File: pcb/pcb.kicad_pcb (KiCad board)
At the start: 2 copper layers, 48 x 60 mm, 51 parts, among them J1 USB_C_Receptacle_USB2.0_14P, J2 LCD, J4 LCD CTRL, J5 Moisture, J6 HC-05, J7 DEBUG, J9 USART3 TX, SW1 PWR SWITCH, U1 TLV62569DBV, U2 STM32F446RETx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

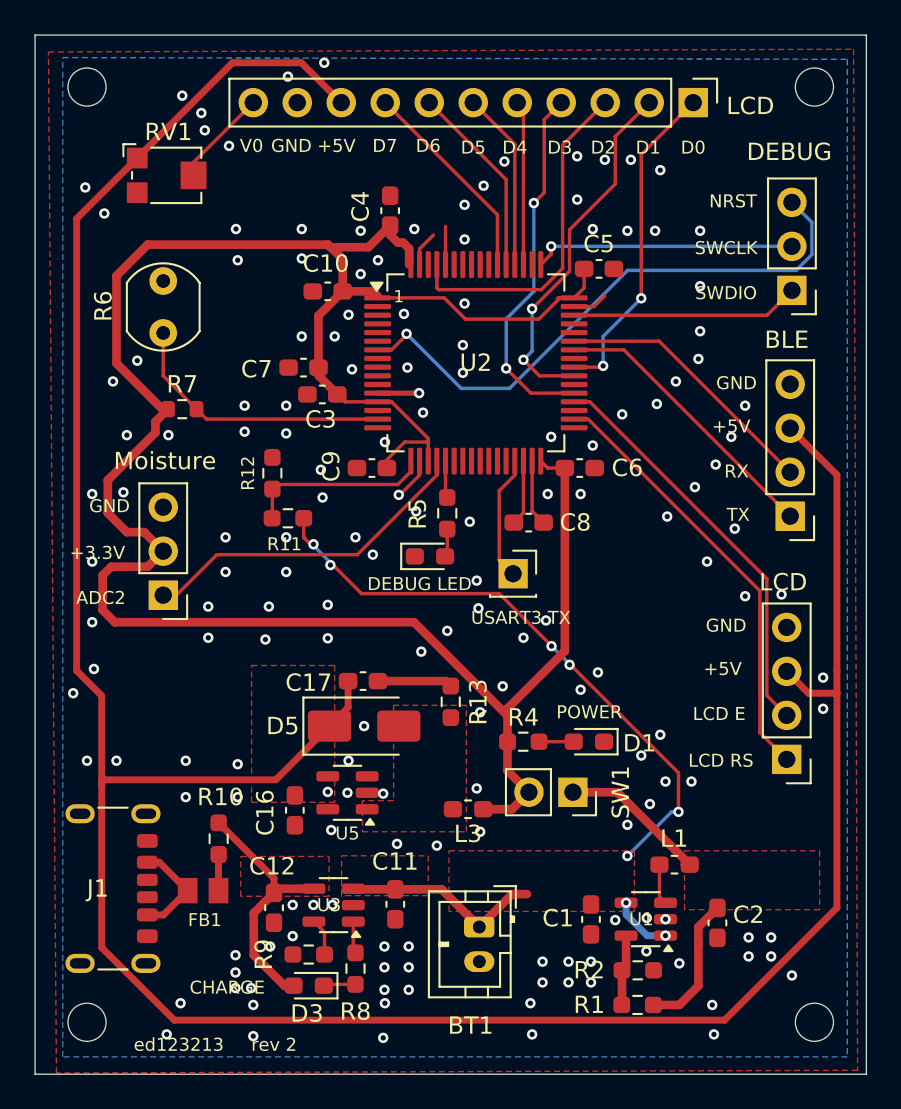
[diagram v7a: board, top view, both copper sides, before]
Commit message: Add more vias
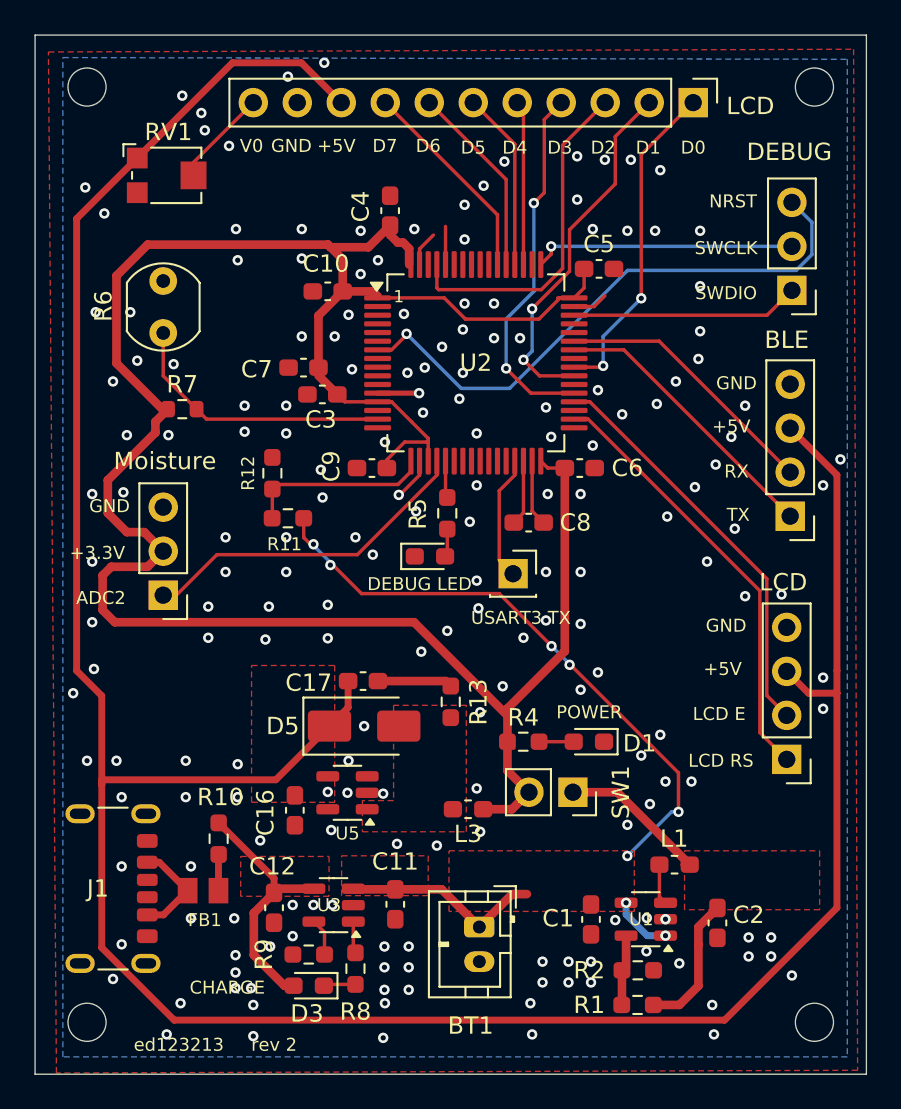
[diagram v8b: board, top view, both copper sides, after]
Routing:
- net GND: vias 166 -> 192
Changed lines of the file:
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@@
+	)
+	(via
+		(at 73 90.5)
+		(size 0.6)
+		(drill 0.3)
+		(layers "F.Cu" "B.Cu")
+		(free yes)
+		(net 1)
+	)
+	(via
+		(at 73 87.5)
+		(size 0.6)
+		(drill 0.3)
+		(layers "F.Cu" "B.Cu")
+		(free yes)
+		(net 1)
 	)
 	(via
@@
 	)
 	(via
+		(at 69 92)
+		(size 0.6)
+		(drill 0.3)
+		(layers "F.Cu" "B.Cu")
+		(free yes)
+		(net 1)
+	)
+	(via
 		(at 78.5 70.5)
 		(size 0.6)
@@
 	)
 	(via
+		(at 69.5 55.5)
+		(size 0.6)
+		(drill 0.3)
+		(layers "F.Cu" "B.Cu")
+		(free yes)
+		(net 1)
+	)
+	(via
 		(at 109.5 76.6)
 		(size 0.6)
@@
 	)
 	(via
+		(at 95.5 70.5)
+		(size 0.6)
+		(drill 0.3)
+		(layers "F.Cu" "B.Cu")
+		(free yes)
+		(net 1)
+	)
+	(via
+		(at 92 57)
+		(size 0.6)
+		(drill 0.3)
+		(layers "F.Cu" "B.Cu")
+		(free yes)
+		(net 1)
+	)
+	(via
 		(at 85.574 93.326)
 		(size 0.6)
@@
 	)
 	(via
+		(at 75.5 90.5)
+		(size 0.6)
+		(drill 0.3)
+		(layers "F.Cu" "B.Cu")
+		(free yes)
+		(net 1)
+	)
+	(via
 		(at 80.9 83.2)
 		(size 0.6)
@@
 	)
 	(via
+		(at 89.5 65.5)
+		(size 0.6)
+		(drill 0.3)
+		(layers "F.Cu" "B.Cu")
+		(free yes)
+		(net 1)
+	)
+	(via
 		(at 89.6 72.6)
 		(size 0.6)
@@
 	)
 	(via
+		(at 67.5 55.5)
+		(size 0.6)
+		(drill 0.3)
+		(layers "F.Cu" "B.Cu")
+		(free yes)
+		(net 1)
+	)
+	(via
 		(at 80.5 64.6)
 		(size 0.6)
@@
 	)
 	(via
+		(at 88.5 60.5)
+		(size 0.6)
+		(drill 0.3)
+		(layers "F.Cu" "B.Cu")
+		(free yes)
+		(net 1)
+	)
+	(via
 		(at 76.1 62.4)
 		(size 0.6)
@@
 	)
 	(via
-		(at 85.5 58.7)
+		(at 86.5 58.7)
 		(size 0.6)
 		(drill 0.3)
@@
 	)
 	(via
+		(at 95.5 73.5)
+		(size 0.6)
+		(drill 0.3)
+		(layers "F.Cu" "B.Cu")
+		(free yes)
+		(net 1)
+	)
+	(via
 		(at 93.5 73.3)
 		(size 0.6)
@@
 	)
 	(via
+		(at 93.5 70.5)
+		(size 0.6)
+		(drill 0.3)
+		(layers "F.Cu" "B.Cu")
+		(free yes)
+		(net 1)
+	)
+	(via
 		(at 75.574 92.626)
 		(size 0.6)
@@
 	)
 	(via
+		(at 77 86)
+		(size 0.6)
+		(drill 0.3)
+		(layers "F.Cu" "B.Cu")
+		(free yes)
+		(net 1)
+	)
+	(via
 		(at 82.0375 83.25)
 		(size 0.6)
@@
 	)
 	(via
+		(at 109.5 65.5)
+		(size 0.6)
+		(drill 0.3)
+		(layers "F.Cu" "B.Cu")
+		(free yes)
+		(net 1)
+	)
+	(via
 		(at 75.7 52.5)
 		(size 0.6)
@@
 	)
 	(via
-		(at 88.7 57.4)
+		(at 88.7 56.5)
 		(size 0.6)
 		(drill 0.3)
@@
 	)
 	(via
+		(at 96.5 60)
+		(size 0.6)
+		(drill 0.3)
+		(layers "F.Cu" "B.Cu")
+		(free yes)
+		(net 1)
+	)
+	(via
 		(at 75.574 94.526)
 		(size 0.6)
@@
 	)
 	(via
+		(at 110.5 64)
+		(size 0.6)
+		(drill 0.3)
+		(layers "F.Cu" "B.Cu")
+		(free yes)
+		(net 1)
+	)
+	(via
 		(at 103.3 64.3)
 		(size 0.6)
@@
 	)
 	(via
+		(at 68.5 94)
+		(size 0.6)
+		(drill 0.3)
+		(layers "F.Cu" "B.Cu")
+		(free yes)
+		(net 1)
+	)
+	(via
 		(at 96.1 94.2)
 		(size 0.6)
@@
 	)
 	(via
+		(at 90.5 55)
+		(size 0.6)
+		(drill 0.3)
+		(layers "F.Cu" "B.Cu")
+		(free yes)
+		(net 1)
+	)
+	(via
 		(at 68.7 81.4)
 		(size 0.6)
@@
 	)
 	(via
+		(at 72 58.5)
+		(size 0.6)
+		(drill 0.3)
+		(layers "F.Cu" "B.Cu")
+		(free yes)
+		(net 1)
+	)
+	(via
+		(at 87.5 57.5)
+		(size 0.6)
+		(drill 0.3)
+		(layers "F.Cu" "B.Cu")
+		(free yes)
+		(net 1)
+	)
+	(via
 		(at 98.2 50.8)
 		(size 0.6)
@@
 	)
 	(via
+		(at 69 83.5)
+		(size 0.6)
+		(drill 0.3)
+		(layers "F.Cu" "B.Cu")
+		(free yes)
+		(net 1)
+	)
+	(via
 		(at 76.6 95.5)
 		(size 0.6)
@@
 	)
 	(via
+		(at 90.5 57)
+		(size 0.6)
+		(drill 0.3)
+		(layers "F.Cu" "B.Cu")
+		(free yes)
+		(net 1)
+	)
+	(via
 		(at 88.8 55)
 		(size 0.6)
@@
 	)
 	(via
+		(at 89.5 62.5)
+		(size 0.6)
+		(drill 0.3)
+		(layers "F.Cu" "B.Cu")
+		(free yes)
+		(net 1)
+	)
+	(via
 		(at 101.2 93.1)
 		(size 0.6)
@@
 	)
 	(via
+		(at 85.5 59)
+		(size 0.6)
+		(drill 0.3)
+		(layers "F.Cu" "B.Cu")
+		(free yes)
+		(net 1)
+	)
+	(via
 		(at 86.175 60.175)
 		(size 0.6)
@@
 	)
 	(via
+		(at 69 87.5)
+		(size 0.6)
+		(drill 0.3)
+		(layers "F.Cu" "B.Cu")
+		(free yes)
+		(net 1)
+	)
+	(via
 		(at 96.1 93)
 		(size 0.6)
@@
 		(size 0.6)
 		(drill 0.3)
+		(layers "F.Cu" "B.Cu")
+		(free yes)
+		(net 1)
+	)
+	(via
+		(at 93.5 61)
+		(size 0.6)
+		(drill 0.3)
